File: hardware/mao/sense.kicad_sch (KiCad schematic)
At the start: 14 parts, among them U401 LSM6DSOXTR, U402 VL53L4CDV0DH/1, U403 OPT3004DNPR

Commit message: hardware: MAO_MAIN A0 routed board, fab package and final review
6-layer JLC06161H-3313 board (F / GND / signals / +3V3 / GND / B), routed from the
design scripts: designed power and fan-out copper, grid router with closed-set A*,
stub pruning, GND stitching (two ties on large pour fragments), tidy.
DRC 0 violations / 0 unconnected / 0 parity; ERC 0; silkscreen checker 0 findings.

- silkscreen: ODD JOBS mark and identity on both faces, S/N box, function-named
  test pads in a 3.0 x 3.2 mm service field; references for every semiconductor and
  connector plus the passives the service docs name, the rest on assembly drawings
- stackup, black mask, white legend and ENIG written into the board
- fab: 6-layer Gerbers + drill, JLC BOM (47 lines, LCSC on every line) and CPL
  (113 parts), assembly PDFs, FAB-NOTES with computed via counts
- docs: PCB, ODD JOBS and order-readiness review sections, final report, renders,
  factory-test pad map, bring-up and architecture updates

Co-Authored-By: Claude Opus 5.5 <noreply@anthropic.com>
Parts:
- R402: LCSC (none) -> C25076; MPN (none) -> 0402WGF1000TCE; Manufacturer (none) -> UNI-ROYAL
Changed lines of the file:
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@@
 			)
 		)
-		(property "MPN" ""
+		(property "MPN" "0402WGF1000TCE"
 			(at 339.09 43.18 0)
 			(effects
@@
 			)
 		)
-		(property "Manufacturer" ""
+		(property "Manufacturer" "UNI-ROYAL"
 			(at 339.09 43.18 0)
 			(effects
@@
 			)
 		)
-		(property "LCSC" ""
+		(property "LCSC" "C25076"
 			(at 339.09 43.18 0)
 			(effects

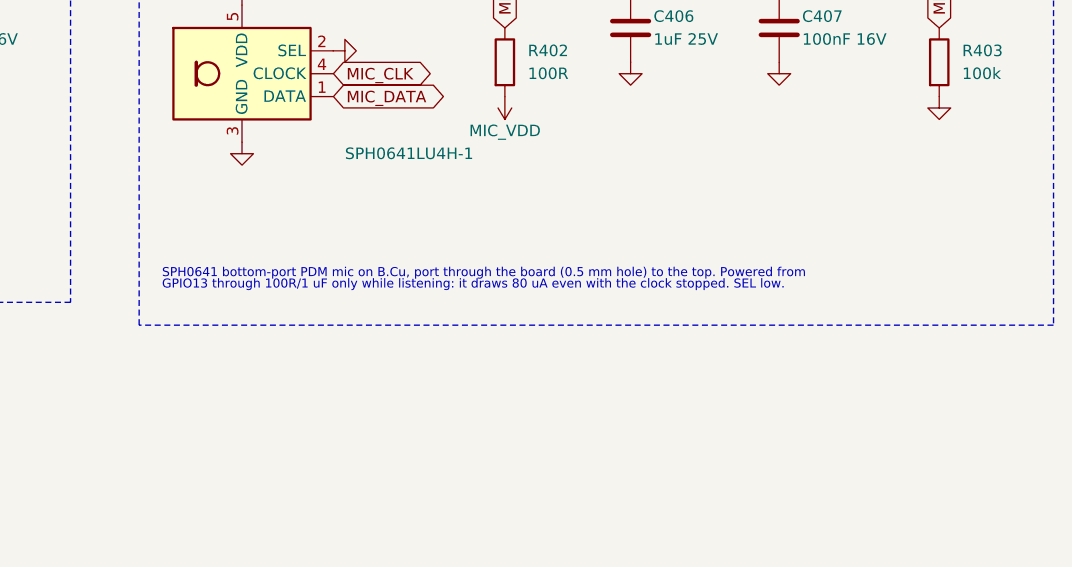
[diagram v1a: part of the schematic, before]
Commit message: hardware: MAO_MAIN A0 4-layer release, plug-in display, ODD JOBS review
- 4 layers (JLC04161H-1080): L1 parts + critical lines, L2 solid GND,
  L3 power regions + slow lines, L4 parts + lines. Re-placed and
  re-routed from scratch: 191 vias (6-layer board: 230).
- J301 HDGC 0.5K-HX-18PWB (C2919497): the round panel plugs in, no
  solder (Winstar 18-pin standard); display TE line added.
- 4-layer pin map; firmware header, pin-map doc and schematic notes
  generated from pinmap.py.
- Pipeline steps: power_regions, plane_check, via_off_pad, snap45 (all
  segments 0/45/90), models3d (datasheet-height bodies for every part).
- Checks: DRC/ERC/parity 0, every L2/L3 plane one piece, silk checker 0,
  Gerbers reviewed independently, firmware 5 configs 0 warnings.
- Mechanical: display standoff 2.7 mm for IR-receiver clearance, ToF
  light-blocking gasket, mic gasket tube, TOP-spring boss; panel tabs at
  2 and 8 o'clock.
- Docs: 4-layer design review, 200-rule ODD JOBS compliance, final
  report, layer plots, Gerber sheet, renders.

Co-Authored-By: Claude Opus 5.5 <noreply@anthropic.com>
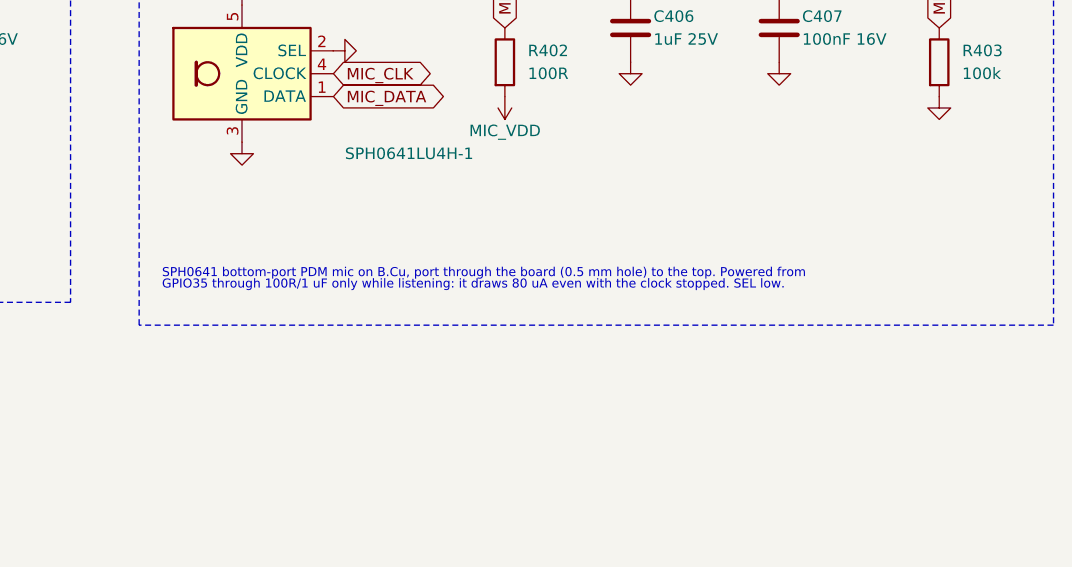
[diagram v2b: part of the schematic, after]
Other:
- note added: "GPIO35 through 100R/1 uF only while listening: it draws 80 uA even with the clock stopped. SEL low."
- note removed: "GPIO13 through 100R/1 uF only while listening: it draws 80 uA even with the clock stopped. SEL low."
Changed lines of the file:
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@@
 		)
 	)
-	(text "GPIO13 through 100R/1 uF only while listening: it draws 80 uA even with the clock stopped. SEL low."
+	(text "GPIO35 through 100R/1 uF only while listening: it draws 80 uA even with the clock stopped. SEL low."
 		(exclude_from_sim no)
 		(at 300.99 68.58 0)

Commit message: MAO A0 schematic: one frame per block, wired local nets, no overprinted names
ODD JOBS audit 2, X8 (rules 187, 188):
- Parts added late (C111, R117, R507) join their block's frame instead of opening a duplicate frame
  with a copy of its note that ran over the neighbours.
- A two-pin part on a net that only joins it to one side pin of its block's IC is wired to that pin
  (the pin's label still names the net, so board, rules and procedures keep their names); feedback and
  UVLO-style dividers hang off their pin as a divider column. Columns step so no wire crosses a part.
- Adjacent pins on one rail share one rail symbol, joined by a wire; a sideways rail symbol keeps its
  name on its own row; turned passives, LEDs and diodes keep their reference and value off the body.
- Rail-source declarations sit in their own frame in the layout flow, not over the title block.
- Two stale notes corrected (C105 distance to VIN, R204 A0 voltage); board fields synced.

ERC 0, DRC 0 / 0 / parity 0.

Co-Authored-By: Claude Opus 5.5 <noreply@anthropic.com>
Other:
- note added: "RAIL SOURCES"
- note added: "SPH0641 bottom-port PDM mic on B.Cu, port through the board (0.5 mm hole) to the top. Powered from GPIO35"
- note added: "VL53L4CD time-of-flight, 0-1.3 m, under the window border. XSHUT from the expander (off by default); GPIO1"
- note added: "open-drain with the 10k pull-up ST recommends. AVDD decoupled 4.7 uF + 100 nF per ST."
- note added: "through 100R/1 uF only while listening: it draws 80 uA even with the clock stopped. SEL low."
- note removed: "GPIO35 through 100R/1 uF only while listening: it draws 80 uA even with the clock stopped. SEL low."
- note removed: "RAIL SOURCE DECLARATIONS"
- note removed: "SPH0641 bottom-port PDM mic on B.Cu, port through the board (0.5 mm hole) to the top. Powered from"
- note removed: "VL53L4CD time-of-flight, 0-1.3 m, under the window border. XSHUT from the expander (off by"
- note removed: "default); GPIO1 open-drain with the 10k pull-up ST recommends. AVDD decoupled 4.7 uF + 100 nF"
- note removed: "per ST."
- moved on the sheet: C403, C404, C405, C406, C407, MK401, R401, R402, R403, U403

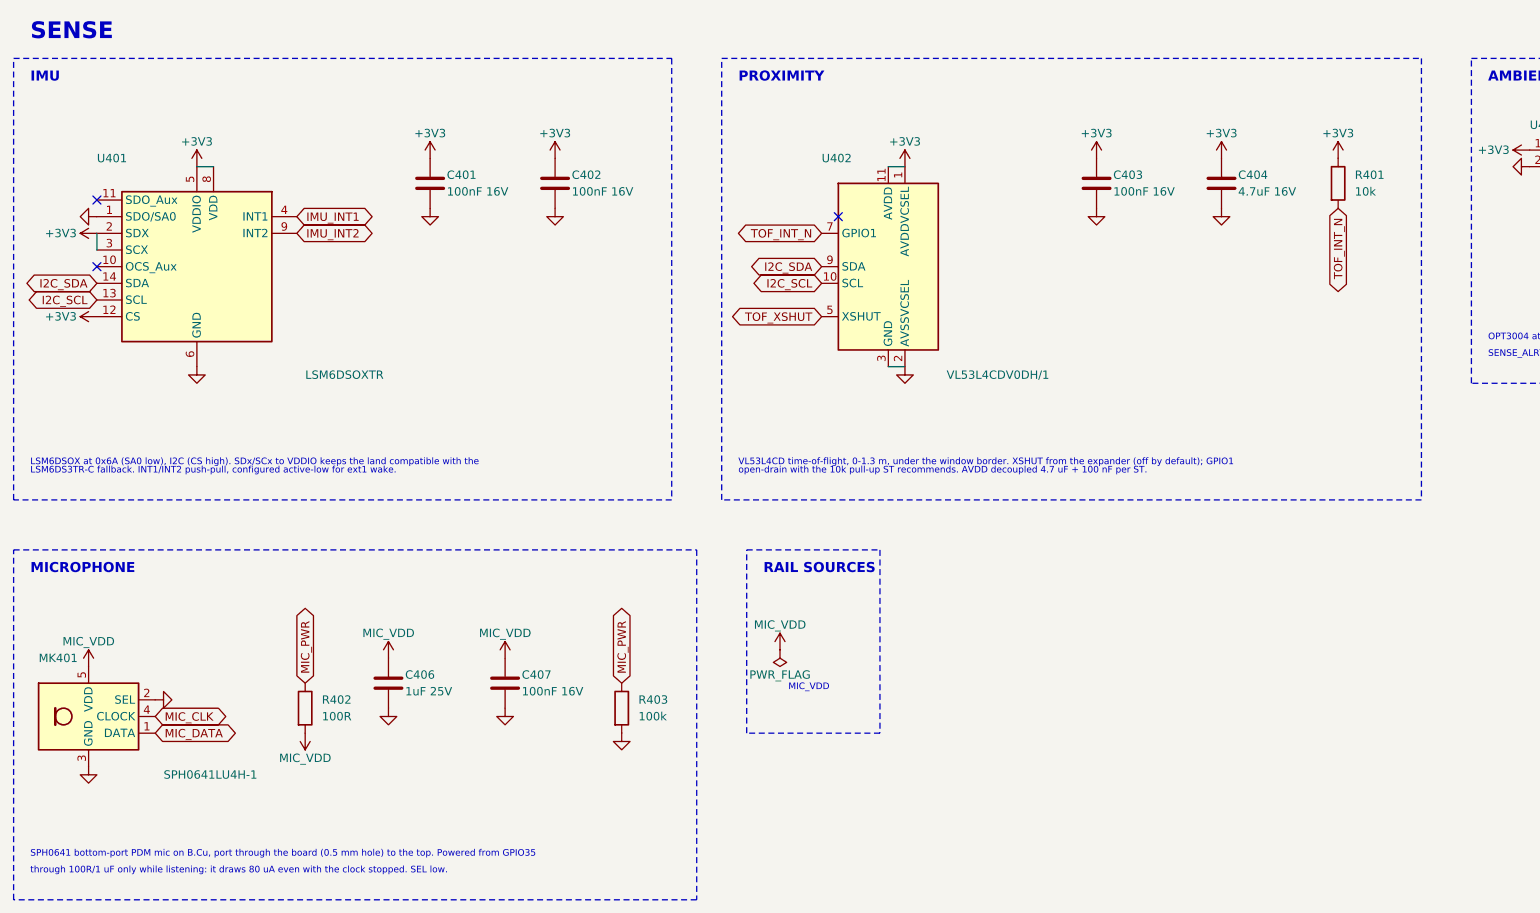
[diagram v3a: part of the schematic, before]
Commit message: MAO A0 audit 3 fixes: VSYS feed un-necked, speaker lines over VSYS, silk leaders to their parts
Electrical audit 3 (no blocker; issue I-1):
- 11 o'clock panel tab 320 -> 328 deg: its keep-out necked the L3 VSYS band to 0.27 mm beside H1
- via-free corner where the VSYS branch turns into the backlight bar (a C205/U202 via left 0.26 mm)
- plane_check: GND and rail regions refilled at 0.5 mm minimum width must not split (necks fail
  the build); the +3V3 mesh is reported
- self-test board_id upper limit 1700 -> 1720 mV (the 3.32 V rail corner reached 1.697 V)
- comments: rail 3.10-3.32 V, AW9364 dropout, TPS22919 turn-on vs rise, panel clock, Kconfig help
- D101 drawn as a unidirectional TVS (zener glyph); module +3V3 via on C202's branch axis

ODD JOBS audit 3 (0 FAIL; recommended fixes):
- VSYS branch extended under both speaker lines (they sat over the VSYS/+3V3 zone gap); LCD_RST_N
  off L3; L3/L4 broadside 17.4 -> 13.8 mm
- EXP_RST_N's leg to TP11 designed on L3 (left to the router it detoured)
- leaders end 0.3 mm off their own part, at least 0.1 mm nearer it than any other part
- no silk text on touch-electrode copper (silk.py, mao_labels.py, check_silk_text.py): REAR and
  MIC moved
- schematic note lines on a 2.54 mm pitch (snapped 2.29 mm printed pairs that touched); tail note
- back identity on a reserved via-free spot; RSSI check with and without the LRA; drawing text
- final board: DRC 0/0/0, planes whole, no rail neck under 0.5 mm, silk 83 texts 0 findings,
  mech 0, 205 vias, 921 segments on 45 degrees; firmware 5 builds 0 warnings, 240 host checks;
  merge patch re-verified on b17187e

Co-Authored-By: Claude Opus 5.5 <noreply@anthropic.com>
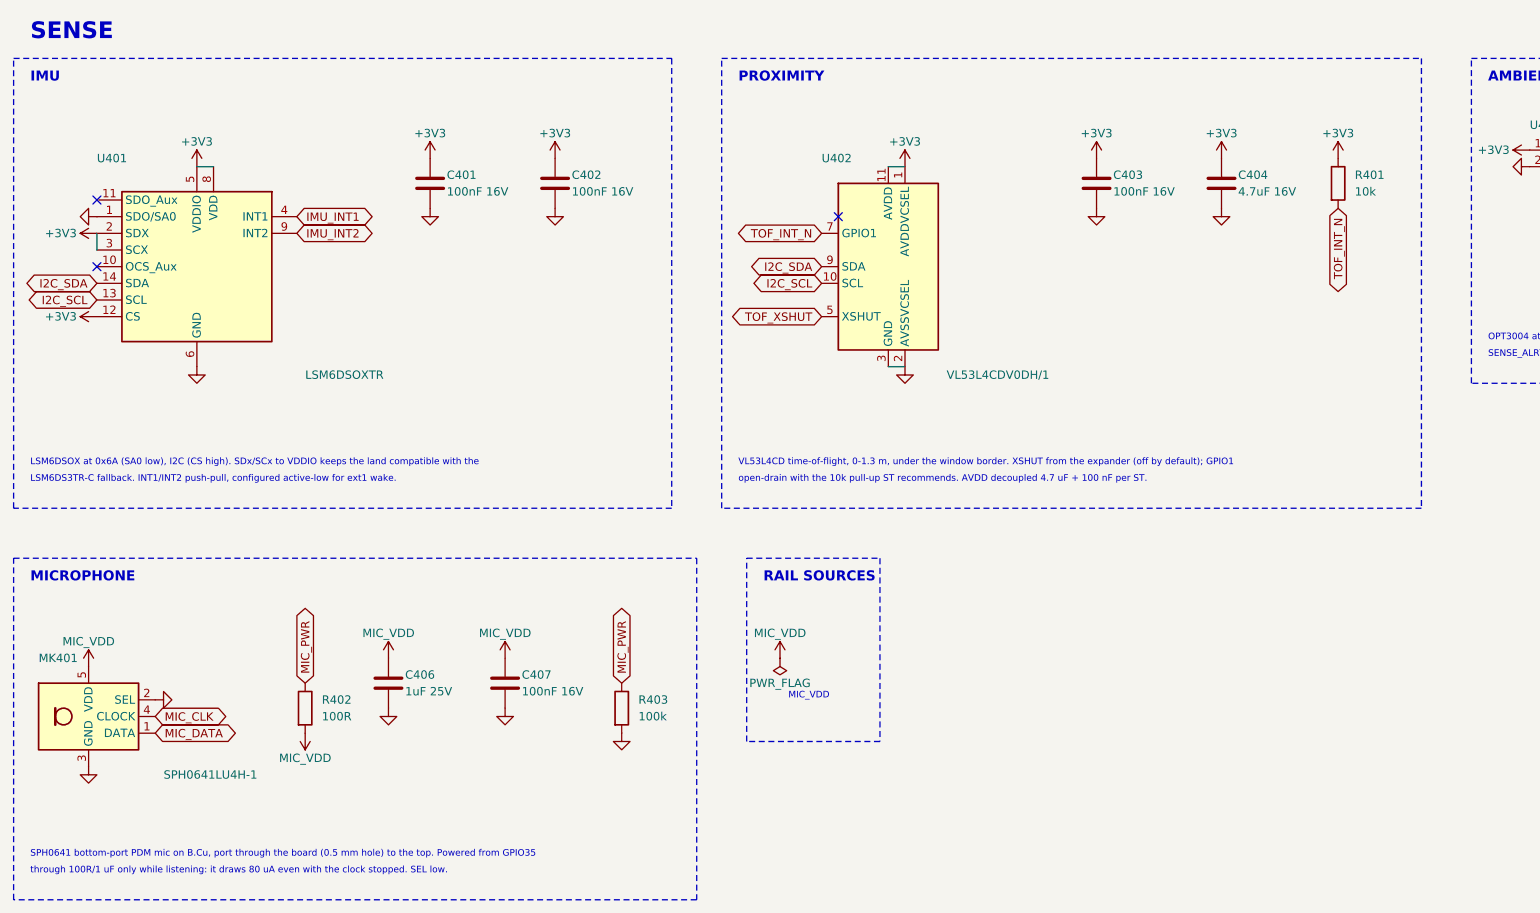
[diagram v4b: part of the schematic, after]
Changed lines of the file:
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@@
 	(rectangle
 		(start 12.7 20.32)
-		(end 113.03 87.63)
+		(end 113.03 88.9)
 		(stroke (width 0.15) (type dash) (color 120 120 120 1))
 		(fill (type none))
@@
 	(text "LSM6DS3TR-C fallback. INT1/INT2 push-pull, configured active-low for ext1 wake."
 		(exclude_from_sim no)
-		(at 15.24 83.82 0)
+		(at 15.24 85.09 0)
 		(effects
 			(font (size 1 1))
@@
 	(rectangle
 		(start 120.65 20.32)
-		(end 227.33 87.63)
+		(end 227.33 88.9)
 		(stroke (width 0.15) (type dash) (color 120 120 120 1))
 		(fill (type none))
@@
 	(text "open-drain with the 10k pull-up ST recommends. AVDD decoupled 4.7 uF + 100 nF per ST."
 		(exclude_from_sim no)
-		(at 123.19 83.82 0)
+		(at 123.19 85.09 0)
 		(effects
 			(font (size 1 1))
@@
 	)
 	(rectangle
-		(start 12.7 95.25)
+		(start 12.7 96.52)
 		(end 116.84 148.59)
 		(stroke (width 0.15) (type dash) (color 120 120 120 1))
@@
 	(text "MICROPHONE"
 		(exclude_from_sim no)
-		(at 15.24 99.06 0)
+		(at 15.24 100.33 0)
 		(effects
 			(font (size 1.524 1.524) (bold yes))
@@
 	)
 	(rectangle
-		(start 124.46 95.25)
-		(end 144.78 123.19)
+		(start 124.46 96.52)
+		(end 144.78 124.46)
 		(stroke (width 0.15) (type dash) (color 120 120 120 1))
 		(fill (type none))
@@
 	(text "RAIL SOURCES"
 		(exclude_from_sim no)
-		(at 127 99.06 0)
+		(at 127 100.33 0)
 		(effects
 			(font (size 1.524 1.524) (bold yes))
@@
 	(symbol
 		(lib_id "MAO:MIC_VDD")
-		(at 129.54 110.49 0)
+		(at 129.54 111.76 0)
 		(unit 1)
 		(exclude_from_sim no)
@@
 		(dnp no)
 		(property "Reference" "#PWR532"
-			(at 129.54 110.49 0)
+			(at 129.54 111.76 0)
 			(effects
 				(font (size 1.27 1.27))
@@
 		)
 		(property "Value" "MIC_VDD"
-			(at 129.54 106.68 0)
-			(effects
-				(font (size 1.27 1.27))
-			)
-		)
-		(property "Footprint" ""
-			(at 129.54 110.49 0)
-			(effects
-				(font (size 1.27 1.27))
-				(hide yes)
-			)
-		)
-		(property "Datasheet" ""
-			(at 129.54 110.49 0)
+			(at 129.54 107.95 0)
+			(effects
+				(font (size 1.27 1.27))
+			)
+		)
+		(property "Footprint" ""
+			(at 129.54 111.76 0)
+			(effects
+				(font (size 1.27 1.27))
+				(hide yes)
+			)
+		)
+		(property "Datasheet" ""
+			(at 129.54 111.76 0)
 			(effects
 				(font (size 1.27 1.27))
@@
 	(symbol
 		(lib_id "power:PWR_FLAG")
-		(at 129.54 110.49 180)
+		(at 129.54 111.76 180)
 		(unit 1)
 		(exclude_from_sim no)
@@
 		(dnp no)
 		(property "Reference" "#FLG533"
-			(at 129.54 110.49 0)
+			(at 129.54 111.76 0)
 			(effects
 				(font (size 1.27 1.27))
@@
 		)
 		(property "Value" "PWR_FLAG"
-			(at 129.54 114.3 0)
-			(effects
-				(font (size 1.27 1.27))
-			)
-		)
-		(property "Footprint" ""
-			(at 129.54 110.49 0)
-			(effects
-				(font (size 1.27 1.27))
-				(hide yes)
-			)
-		)
-		(property "Datasheet" ""
-			(at 129.54 110.49 0)
+			(at 129.54 115.57 0)
+			(effects
+				(font (size 1.27 1.27))
+			)
+		)
+		(property "Footprint" ""
+			(at 129.54 111.76 0)
+			(effects
+				(font (size 1.27 1.27))
+				(hide yes)
+			)
+		)
+		(property "Datasheet" ""
+			(at 129.54 111.76 0)
 			(effects
 				(font (size 1.27 1.27))
@@
 	(text "MIC_VDD"
 		(exclude_from_sim no)
-		(at 130.81 116.84 0)
+		(at 130.81 118.11 0)
 		(effects
 			(font (size 1 1))
